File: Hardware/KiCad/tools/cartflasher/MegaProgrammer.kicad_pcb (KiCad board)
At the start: 4 copper layers, 89 x 93 mm, 34 parts, among them J1 USB_C_Receptacle_USB2.0, J2 ICSP, SW1 SW_Push, U1 ATmega2560-16A, U3 FT232RL, Y1 Crystal_GND24

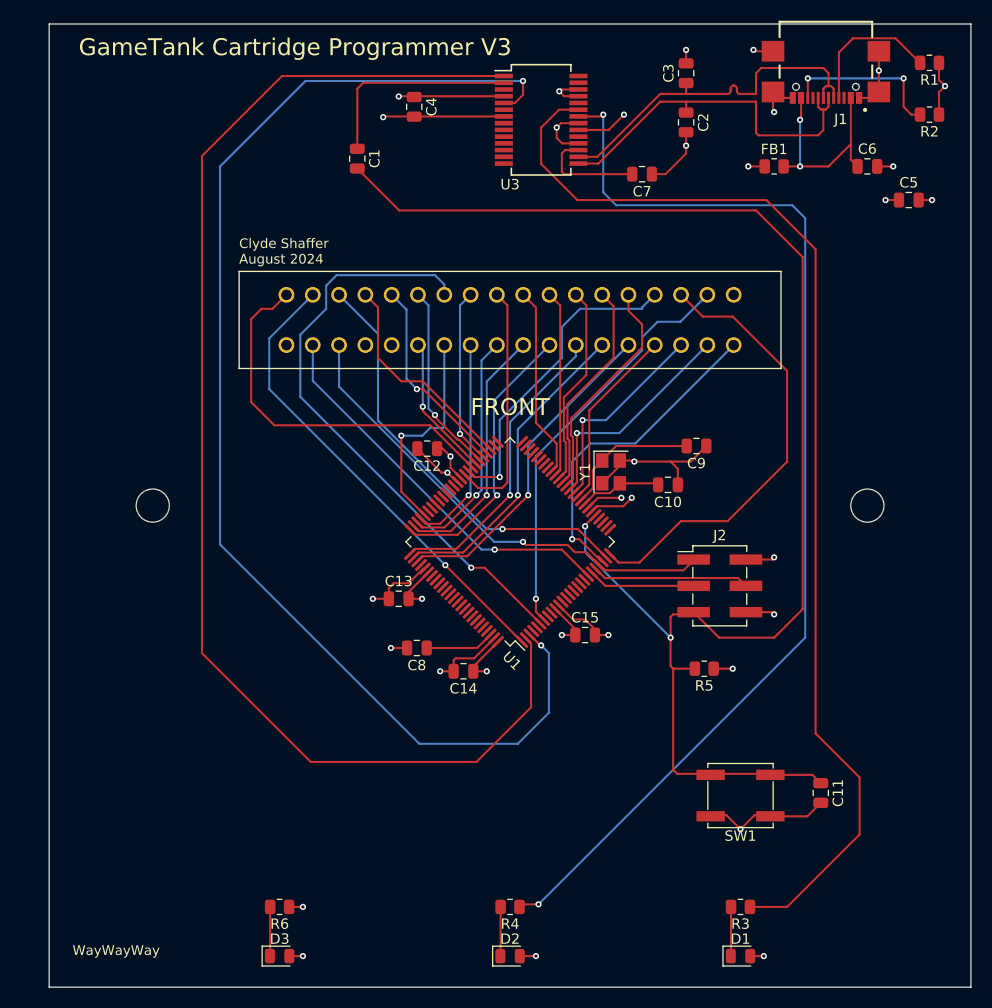
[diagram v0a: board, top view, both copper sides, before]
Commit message: update graphics on flasher v3
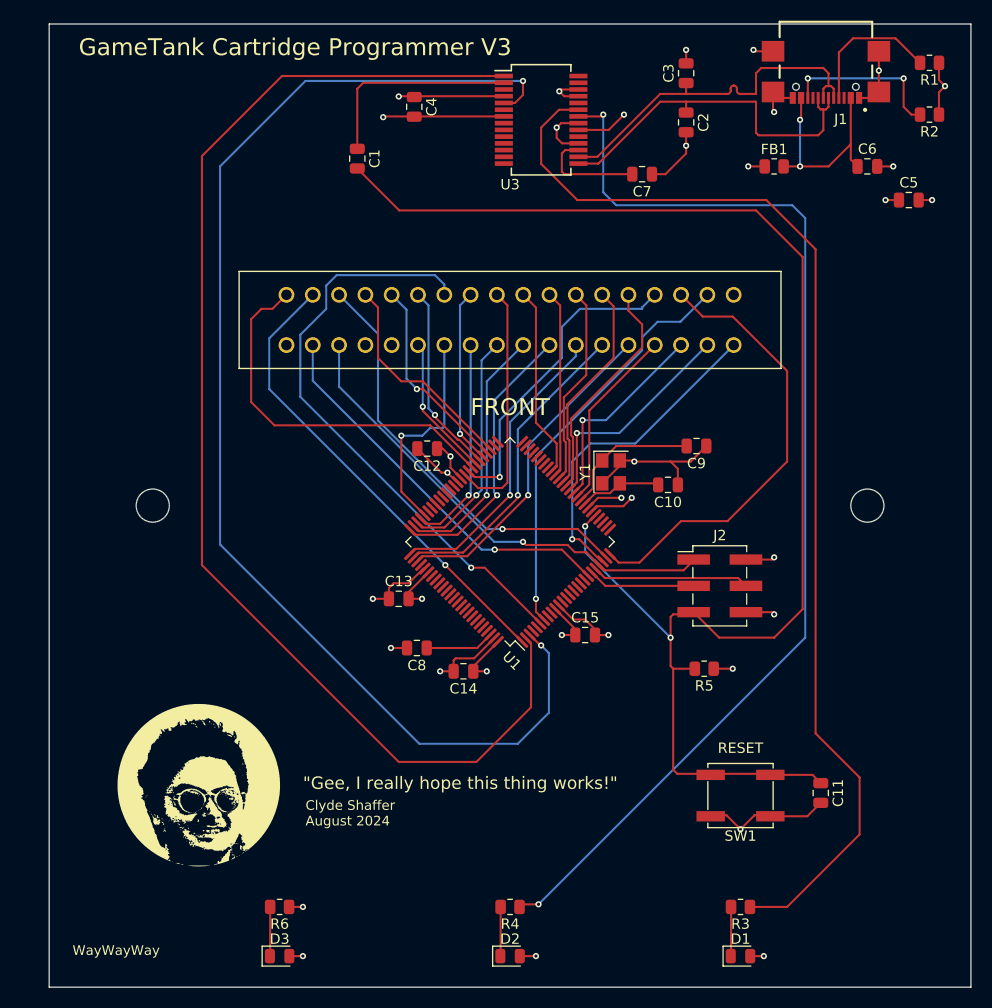
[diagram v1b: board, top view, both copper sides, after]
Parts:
- added G***: LOGO, MegaProgrammer:LogoSeal_neg, F.Cu at (114.5, 133.5)
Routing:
- net /fromHOST: track 125.5 -> 120.6 mm
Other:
- board text added: "RESET"
- board text added: "{dblquote}Gee, I really hope this thing works!{dblquote}"

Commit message: fix unconnected nets in flasher3
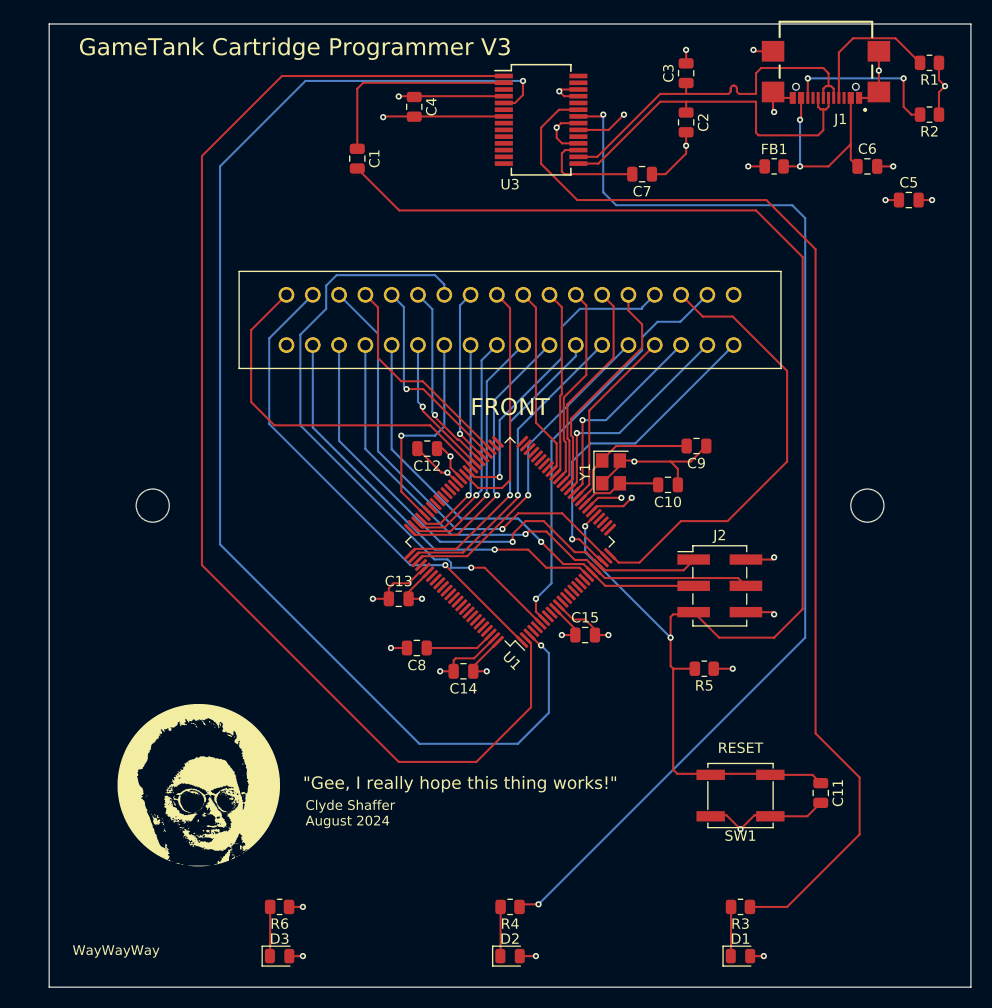
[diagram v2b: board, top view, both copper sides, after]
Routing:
- net /MOSI: track 15.2 -> 52.5 mm, vias 0 -> 1
- net /SCK: track 10.4 -> 44.7 mm, vias 0 -> 1
- net /MISO: track 46.1 -> 51.2 mm
- net /~{IRQ}: track 41.2 -> 44.2 mm
- net /SS: track 37.8 -> 40.5 mm
- net /~{WE}: track 45.4 -> 47.4 mm
- net /~{OE}: track 57.2 -> 59.2 mm
- net /A13: track 36.3 -> 35.7 mm
- net /A9: track 19.4 -> 20.0 mm
